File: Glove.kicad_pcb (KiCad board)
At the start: 4 copper layers, 72.8 x 52 mm, 42 parts, among them J1 USB_C_Receptacle_USB2.0, J2 Joystick, Q1 2N7002, Q2 2N7002, U1 LM1117-3.3, U2 ESP32-WROOM-32D, U3 CP2102N-Axx-xQFN24

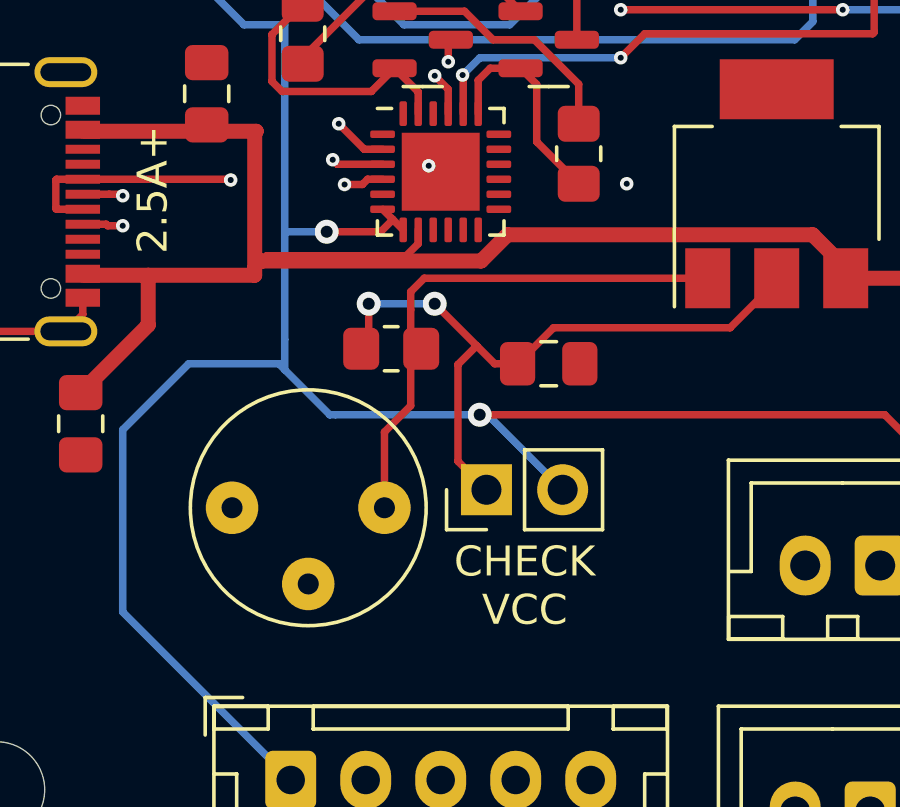
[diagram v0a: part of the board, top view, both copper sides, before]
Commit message: Remove Voltage Divider from Power Supply
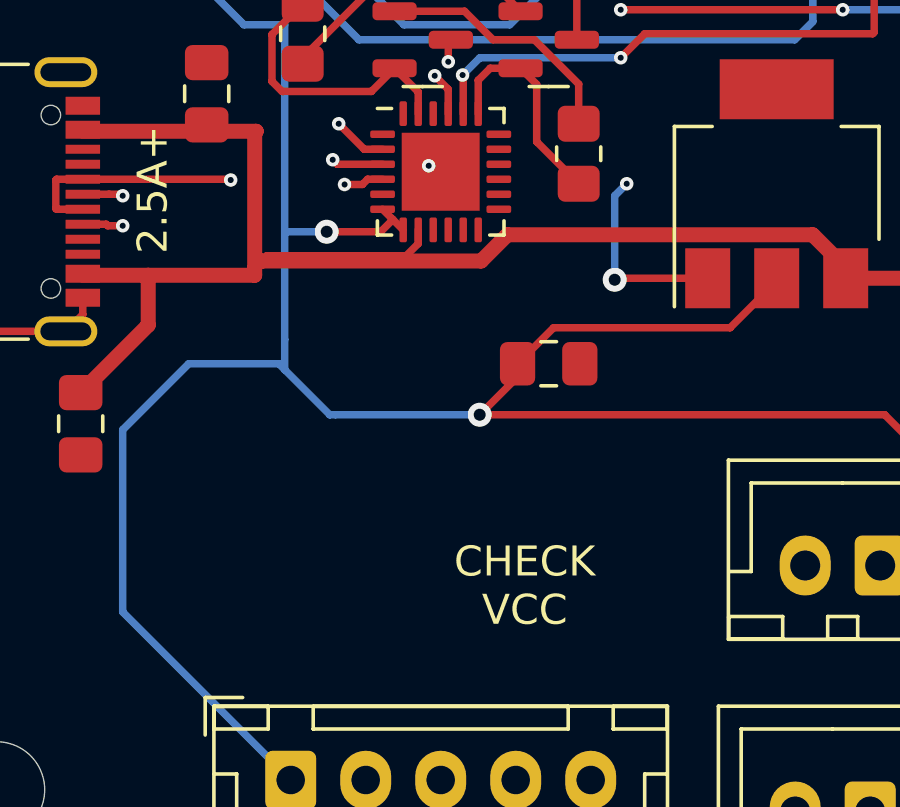
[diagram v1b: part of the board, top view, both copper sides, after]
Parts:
- removed JP1: Jumper_2_Bridged, Connector_PinHeader_2.54mm:PinHeader_1x02_P2.54mm_Vertical
- removed R1: 121, Resistor_SMD:R_0805_2012Metric_Pad1.20x1.40mm_HandSolder
- removed R2: 1k, Potentiometer_THT:Potentiometer_Bourns_3339P_Vertical_HandSoldering
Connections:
- C_Out1 pad 1: Net-(C_Out1-Pad1) -> +3V3
- U1 pad 1: Net-(R1-Pad2) -> GND
- U1 pad 2: Net-(C_Out1-Pad1) -> +3V3
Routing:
- net Net-(C_Out1-Pad1): track 22.7 -> 0.00 mm, vias 2 -> 0
- net Net-(R1-Pad2): track 17.6 -> 0.00 mm
- net +3V3: track 162.1 -> 170.4 mm
- net GND: track 7.20 -> 13.7 mm, vias 6 -> 7

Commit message: Connect VIO to 3.3v for CP2102 chip
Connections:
- U3 pad 5: unconnected-(U3-Pad5) -> +3V3
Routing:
- net +3V3: track 170.4 -> 170.9 mm

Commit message: Add 5.1k Pulldown for CC1 and CC2
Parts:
- added R1: 5.1k, Resistor_SMD:R_0805_2012Metric_Pad1.20x1.40mm_HandSolder, F.Cu at (122.5, 91.0)
- added R2: 5.1k, Resistor_SMD:R_0805_2012Metric_Pad1.20x1.40mm_HandSolder, F.Cu at (122.5, 88.5)
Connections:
- J1 pad A5: unconnected-(J1-PadA5) -> Net-(J1-PadA5)
- J1 pad B5: unconnected-(J1-PadB5) -> Net-(J1-PadB5)
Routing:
- net Net-(J1-PadA5): track 0.00 -> 8.43 mm, vias 0 -> 2
- net Net-(J1-PadB5): track 0.00 -> 7.83 mm, vias 0 -> 2

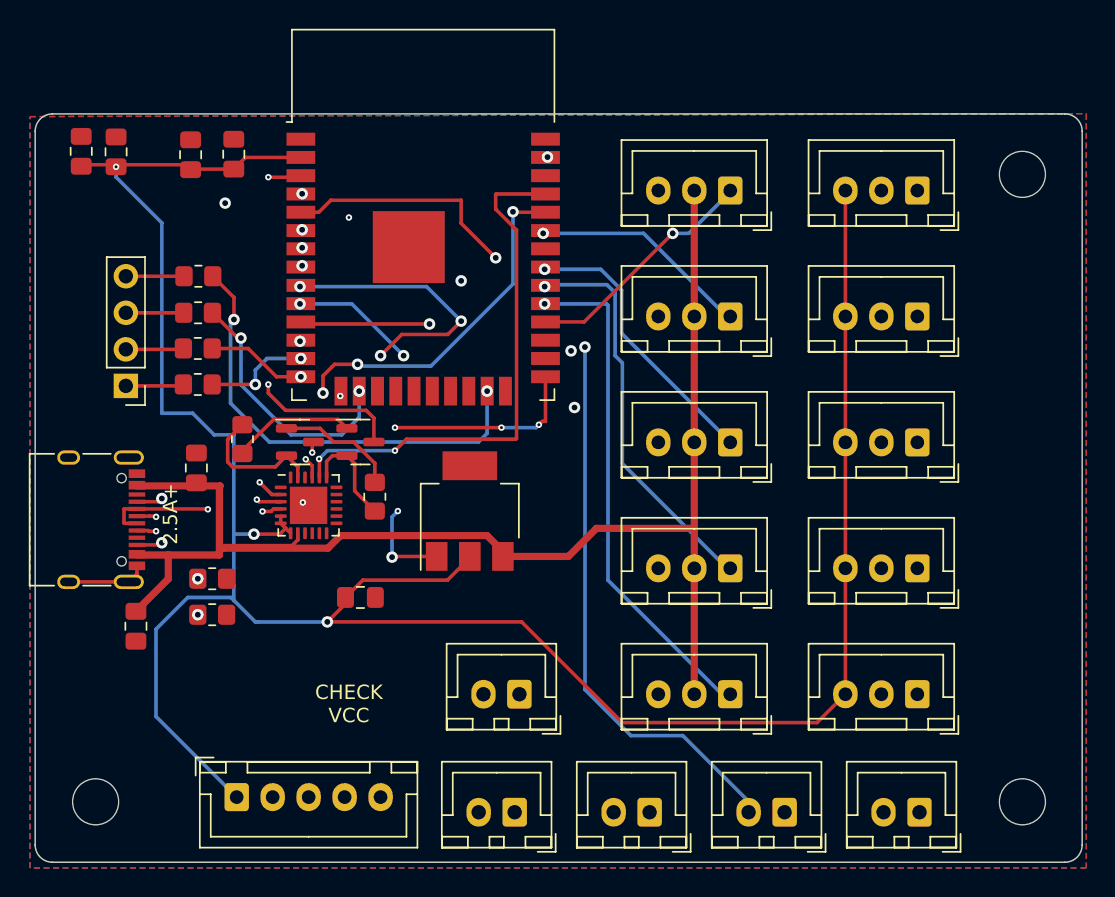
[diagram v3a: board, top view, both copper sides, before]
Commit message: Remove in-pad vias and add 1k pullup for CP2102 RST
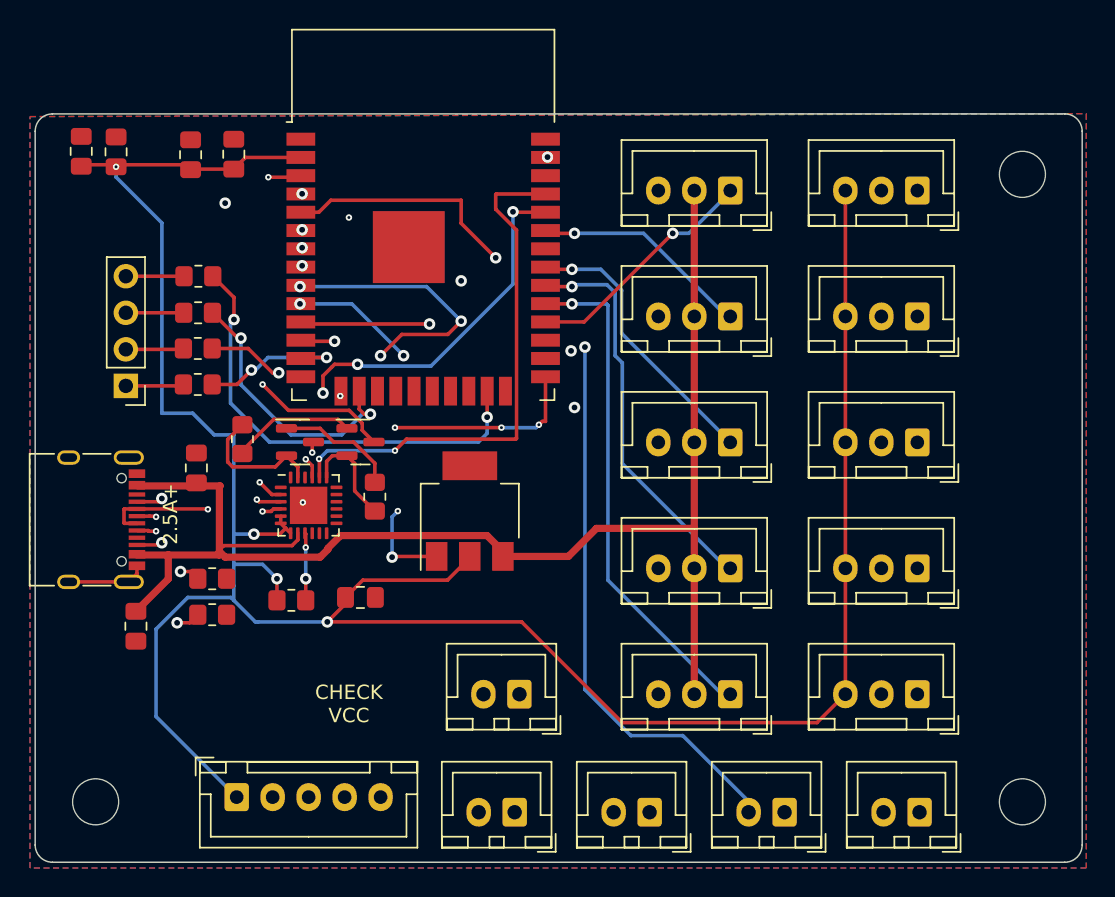
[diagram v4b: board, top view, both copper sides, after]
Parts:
- added R9: 1k, Resistor_SMD:R_0805_2012Metric_Pad1.20x1.40mm_HandSolder, F.Cu at (128.0, 90.0)
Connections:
- U3 pad 9: unconnected-(U3-Pad9) -> Net-(U3-Pad9)
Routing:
- net +3V3: track 170.9 -> 175.8 mm, vias 3 -> 4
- net Net-(U3-Pad9): track 0.00 -> 4.68 mm, vias 0 -> 2
- net Net-(J1-PadB5): track 7.83 -> 9.47 mm
- net Net-(J1-PadA5): track 8.43 -> 9.84 mm
- net BtnB: track 73.9 -> 75.2 mm
- net BtnGrab: track 53.1 -> 54.3 mm
- net +5V: track 97.1 -> 97.8 mm
- net MiddlePot: track 53.4 -> 54.0 mm

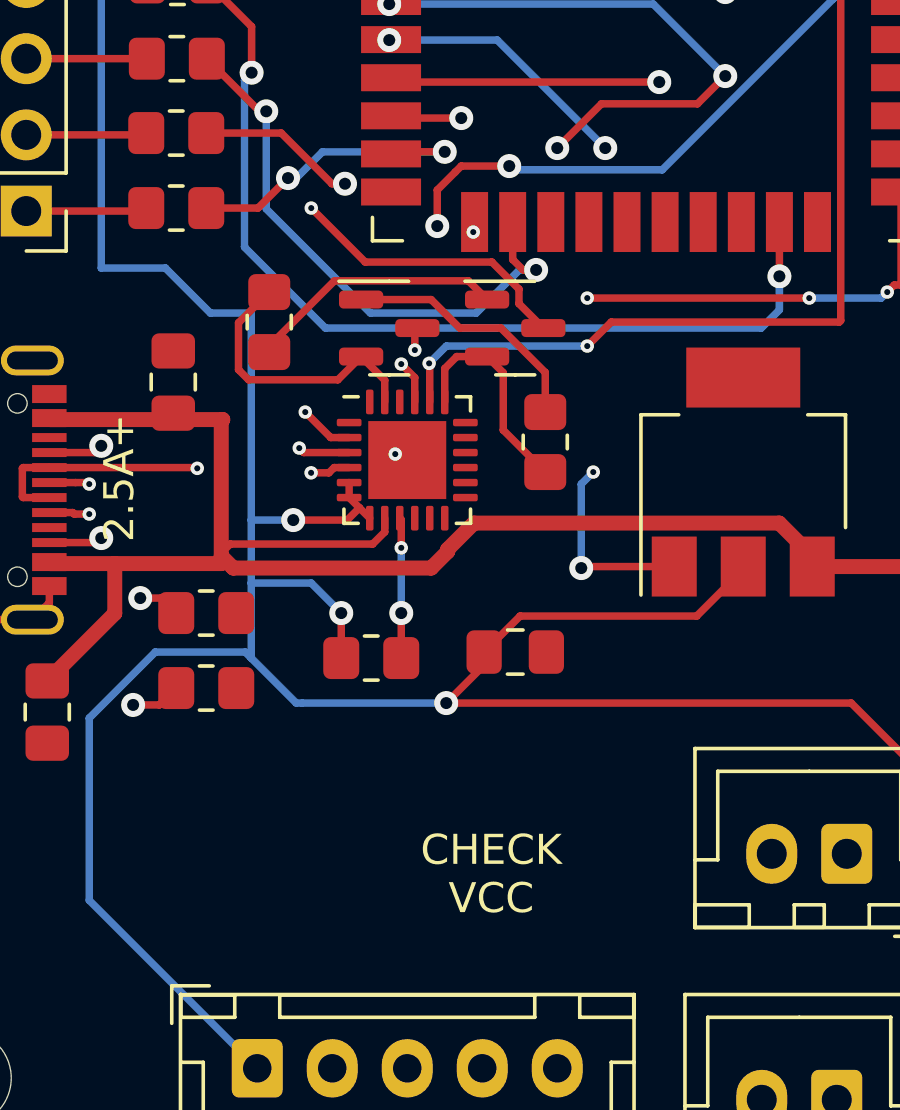
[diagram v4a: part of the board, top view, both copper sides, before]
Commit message: Remove CHECK VCC silkscreen
Signed-off-by: Kozova1 <mug66kk@gmail.com>
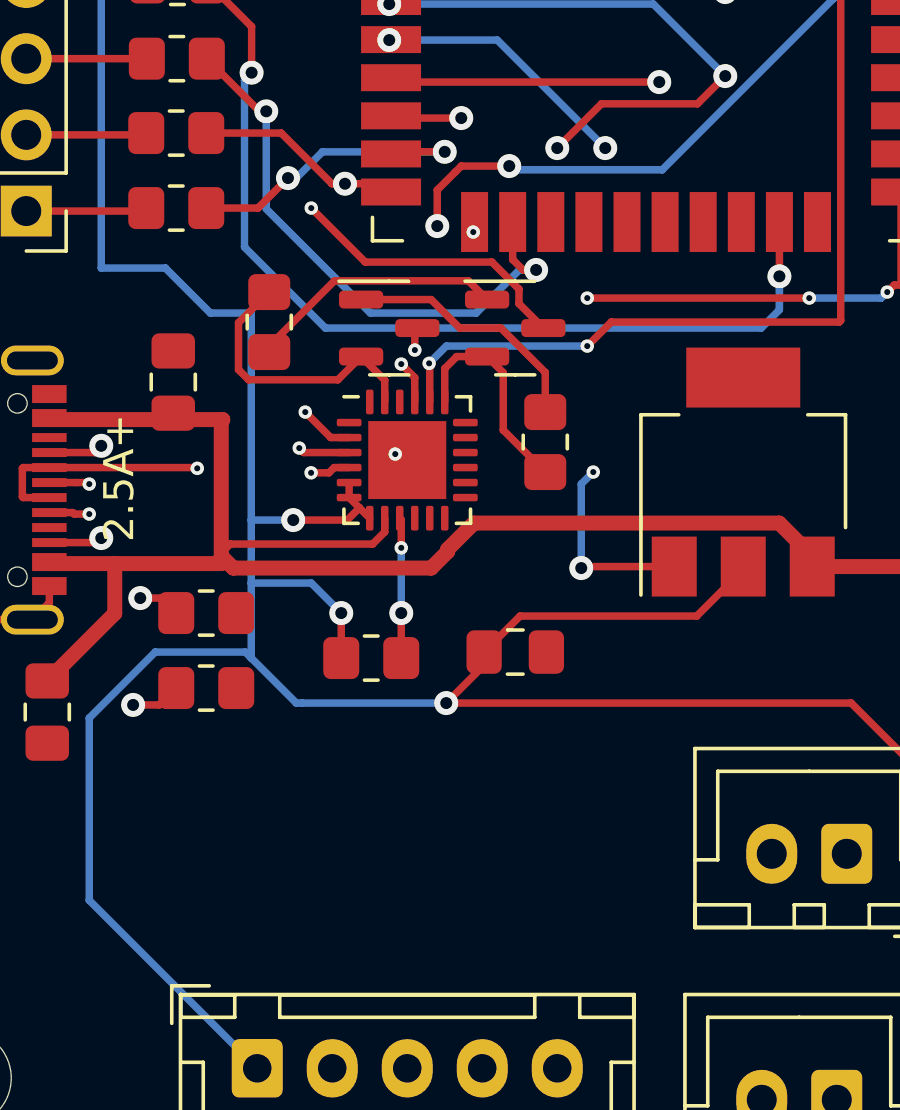
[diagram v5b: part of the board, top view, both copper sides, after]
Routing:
- net BtnTrigger: track 39.0 -> 40.6 mm
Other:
- board text removed: "CHECK VCC"
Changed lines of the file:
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@@
     (fp_line (start 1 0.625) (end -1 0.625) (layer "F.Fab") (width 0.1))
     (fp_line (start -1 0.625) (end -1 -0.625) (layer "F.Fab") (width 0.1))
-    (pad "1" smd roundrect (at -1 0) (size 1.2 1.4) (layers "F.Cu" "F.Paste" "F.Mask") (roundrect_rratio 0.208333)
+    (pad "1" smd roundrect (at -1 0) (size 1.2 1.4) (layers "F.Cu" "F.Paste" "F.Mask") (roundrect_rratio 0.2083333333)
       (net 8 "+3V3") (pintype "passive"))
-    (pad "2" smd roundrect (at 1 0) (size 1.2 1.4) (layers "F.Cu" "F.Paste" "F.Mask") (roundrect_rratio 0.208333)
+    (pad "2" smd roundrect (at 1 0) (size 1.2 1.4) (layers "F.Cu" "F.Paste" "F.Mask") (roundrect_rratio 0.2083333333)
       (net 64 "Net-(U3-Pad9)") (pintype "passive"))
     (model "${KICAD6_3DMODEL_DIR}/Resistor_SMD.3dshapes/R_0805_2012Metric.wrl"
@@
   (gr_text "A" (at 151.538095 102.4) (layer "B.SilkS")
     (effects (font (size 1 1) (thickness 0.15)) (justify mirror))
-  )
-  (gr_text "CHECK\nVCC" (at 132 97.2) (layer "F.SilkS")
-    (effects (font (size 1 1) (thickness 0.15)))
   )
   (gr_text "2.5A+" (at 119.6 84 90) (layer "F.SilkS")
@@
   (segment (start 126.689533 74.189533) (end 125 72.5) (width 0.25) (layer "F.Cu") (net 6))
   (segment (start 127.1245 74.189533) (end 126.689533 74.189533) (width 0.25) (layer "F.Cu") (net 6))
+  (segment (start 127.1245 74.189533) (end 128.384533 74.189533) (width 0.25) (layer "F.Cu") (net 6))
+  (segment (start 128.384533 74.189533) (end 128.66 74.465) (width 0.25) (layer "F.Cu") (net 6))
   (via (at 127.1245 74.189533) (size 0.8) (drill 0.4) (layers "F.Cu" "B.Cu") (net 6))
   (segment (start 138.44952 76.278802) (end 138.44952 93.62452) (width 0.25) (layer "In2.Cu") (net 6))

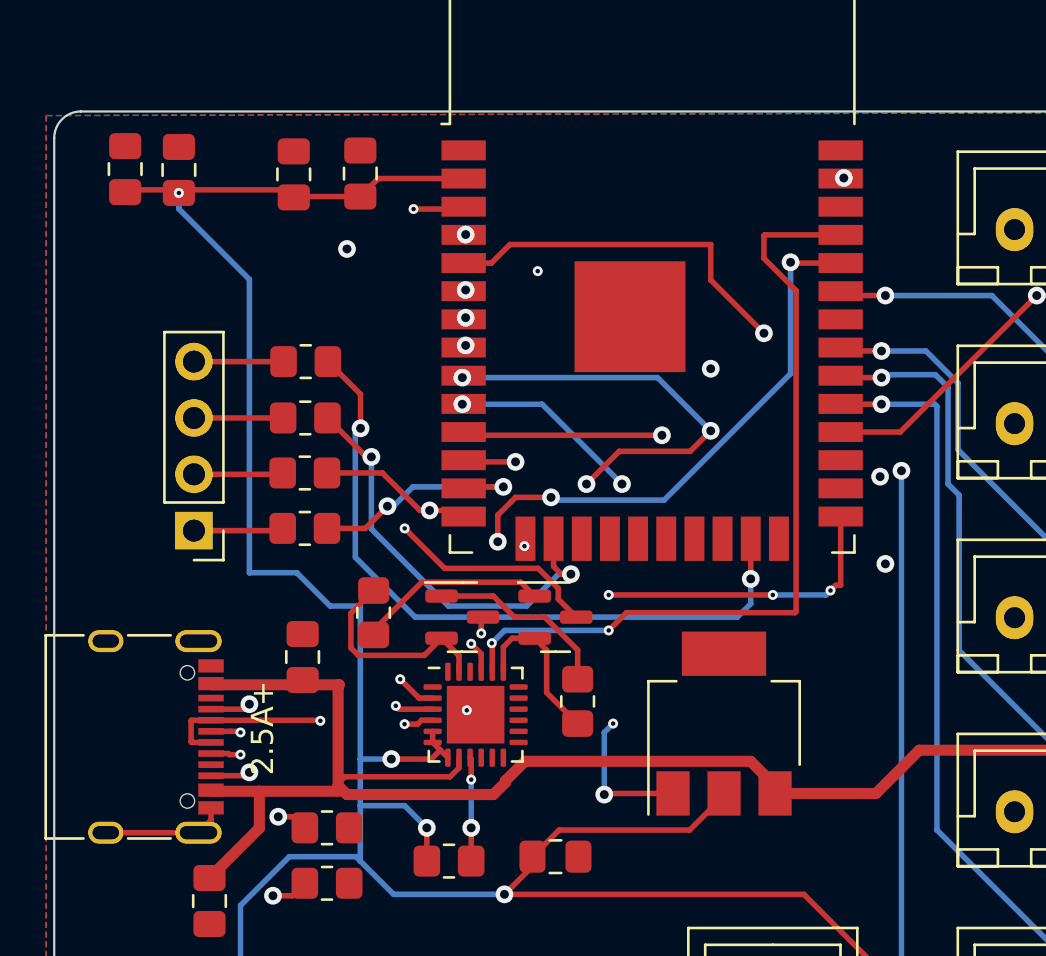
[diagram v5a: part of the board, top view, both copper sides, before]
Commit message: Move decoupling capacitors
Signed-off-by: Kozova1 <mug66kk@gmail.com>
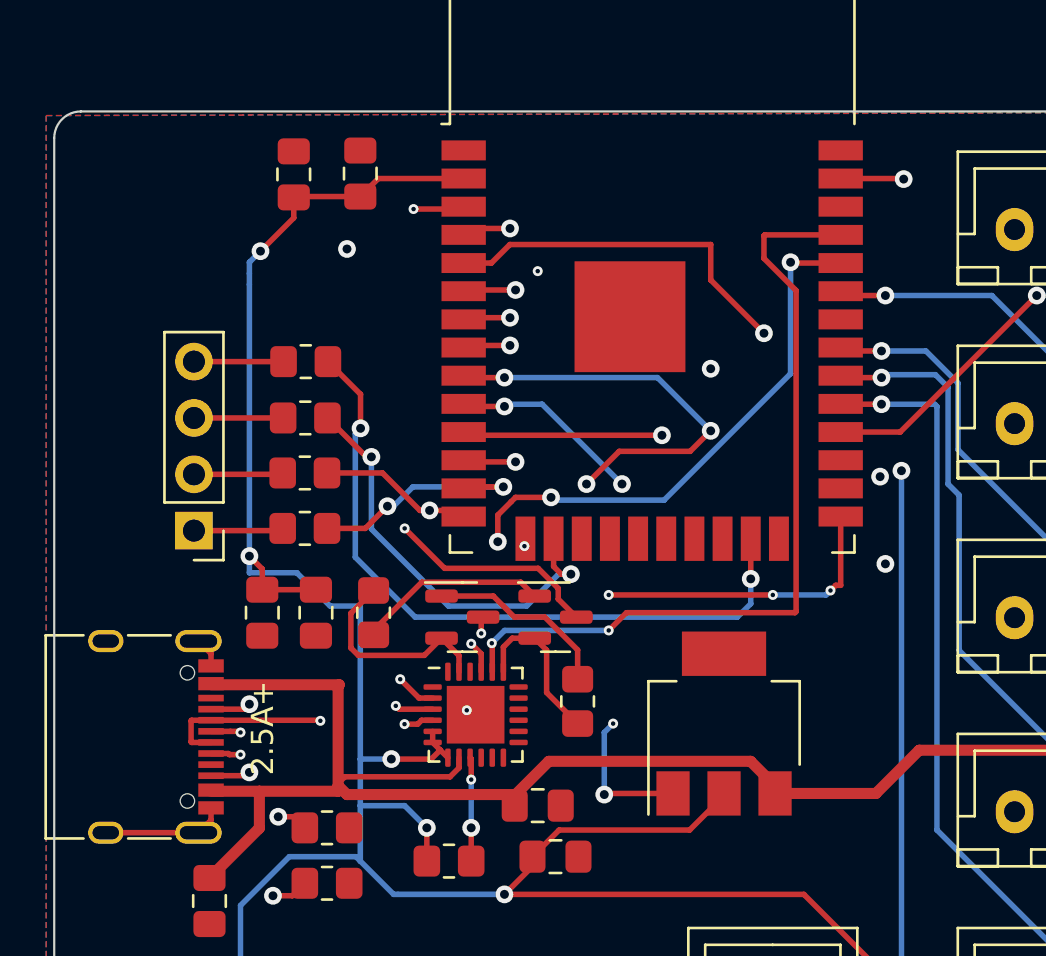
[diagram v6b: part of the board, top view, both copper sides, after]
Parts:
- moved C4 21.8 mm to (122.0, 78.8), turned to -90 degrees
- moved C5 20.3 mm to (119.6, 78.8), turned to -90 degrees
- moved C_In1 12.5 mm to (132.0, 87.5), turned to 0 degrees
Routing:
- net +3V3: track 175.8 -> 171.5 mm, vias 4 -> 5
- net GND: track 13.7 -> 15.2 mm

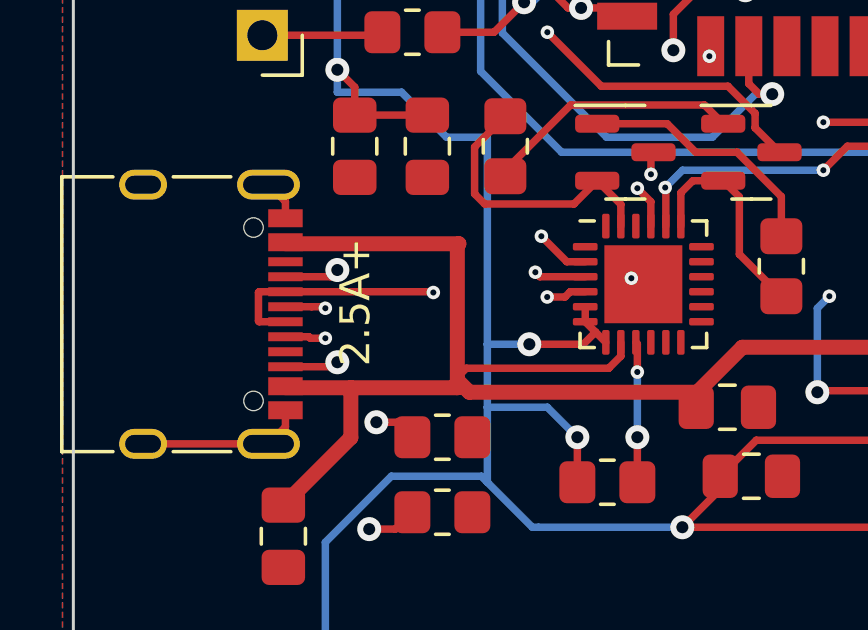
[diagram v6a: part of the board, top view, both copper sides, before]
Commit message: Route D- and D+ as differential pair
Signed-off-by: David Vogman <davidv@edgegaming.gg>
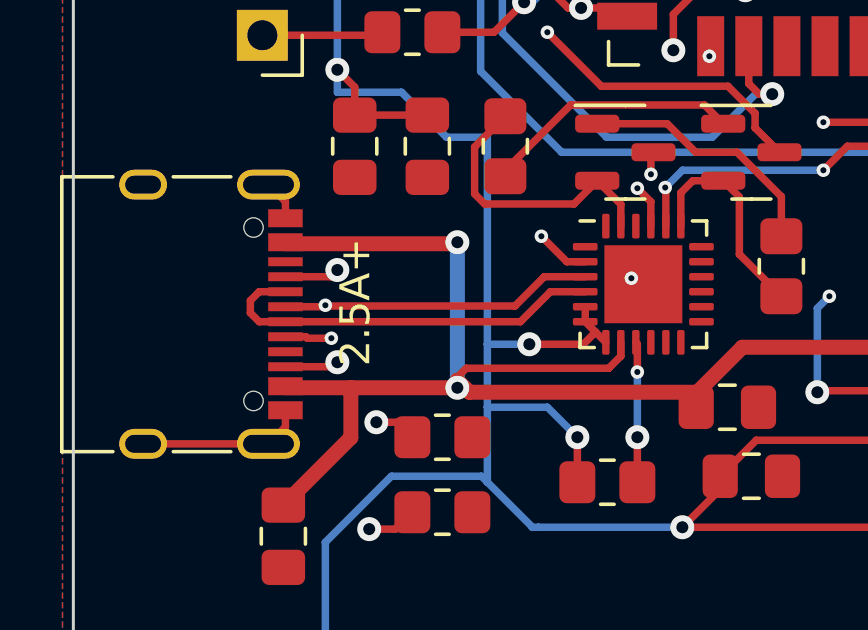
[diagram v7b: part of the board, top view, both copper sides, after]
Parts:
- C_Out1: value 100uF -> 10uF
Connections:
- net Net-(J1-PadA6) renamed /D+
- net Net-(J1-PadA7) renamed /D-
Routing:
- net /D+: track 12.9 -> 13.5 mm, vias 3 -> 2
- net /D-: track 12.9 -> 13.4 mm, vias 2 -> 0
- net +5V: track 97.8 -> 98.1 mm, vias 0 -> 2
